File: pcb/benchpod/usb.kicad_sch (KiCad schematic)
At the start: 24 parts, among them U57 TPS259470ARPWR

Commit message: switched D1, added rules area with keepout
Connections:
- net +5V_EFUSE: now also D1.1 (K); no longer D1.2 (A)
- net GND: now also D1.2 (A); no longer D1.1 (K)
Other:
- moved on the sheet: D1
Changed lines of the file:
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@@
 	(symbol
 		(lib_id "lcsc_lib:SMAJ5.0A_C2925443")
-		(at 48.26 86.36 180)
+		(at 48.26 86.36 0)
 		(unit 1)
 		(body_style 1)
@@
 		)
 		(property "Footprint" "lcsc:SMA_L4.3-W2.6-LS5.0-RD"
-			(at 48.26 78.74 0)
+			(at 48.26 93.98 0)
 			(hide yes)
 			(show_name no)
@@
 		)
 		(property "Datasheet" "https://www.lcsc.com/datasheet/C2925443.pdf"
-			(at 48.26 76.2 0)
+			(at 48.26 96.52 0)
 			(hide yes)
 			(show_name no)
@@
 		)
 		(property "Manufacturer" "Liown(里阳半导体)"
-			(at 48.26 73.66 0)
+			(at 48.26 99.06 0)
 			(hide yes)
 			(show_name no)
@@
 		)
 		(property "MPN" "SMAJ5.0A"
-			(at 48.26 71.12 0)
+			(at 48.26 101.6 0)
 			(hide yes)
 			(show_name no)
@@
 		)
 		(property "LCSC Part" "C2925443"
-			(at 48.26 68.58 0)
+			(at 48.26 104.14 0)
 			(hide yes)
 			(show_name no)

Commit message: route cleanups and out of stock component replacement
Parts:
- C91, C92: footprint Capacitor_SMD:C_0603_1608Metric -> Capacitor_SMD:C_0805_2012Metric; LCSC C59461 -> C45783
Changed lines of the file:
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@@
 			)
 		)
-		(property "Footprint" "Capacitor_SMD:C_0603_1608Metric"
+		(property "Footprint" "Capacitor_SMD:C_0805_2012Metric"
 			(at 174.9552 148.59 0)
 			(hide yes)
@@
 			)
 		)
-		(property "LCSC" "C59461"
+		(property "LCSC" "C45783"
 			(at 173.99 144.78 0)
 			(hide yes)
@@
 			)
 		)
-		(property "Footprint" "Capacitor_SMD:C_0603_1608Metric"
+		(property "Footprint" "Capacitor_SMD:C_0805_2012Metric"
 			(at 186.3852 148.59 0)
 			(hide yes)
@@
 			)
 		)
-		(property "LCSC" "C59461"
+		(property "LCSC" "C45783"
 			(at 185.42 144.78 0)
 			(hide yes)

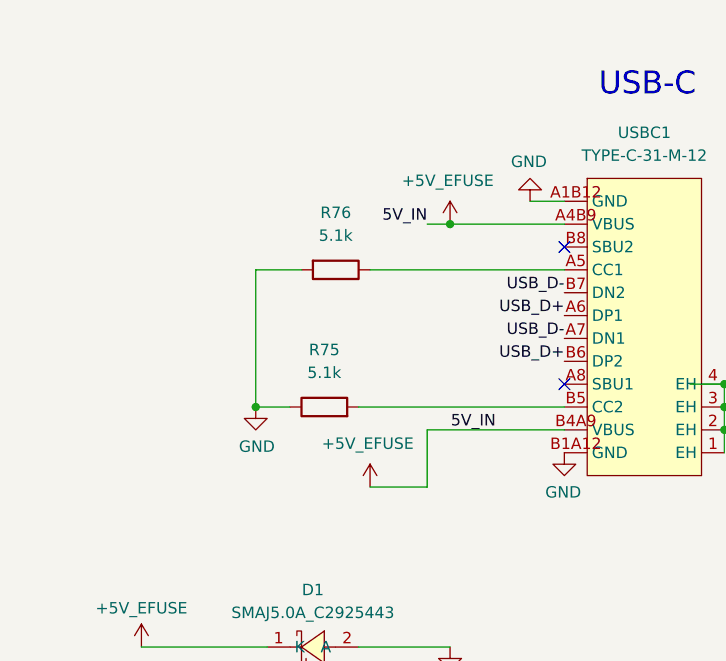
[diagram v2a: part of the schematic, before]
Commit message: fb changes, cc sensing, cleanups
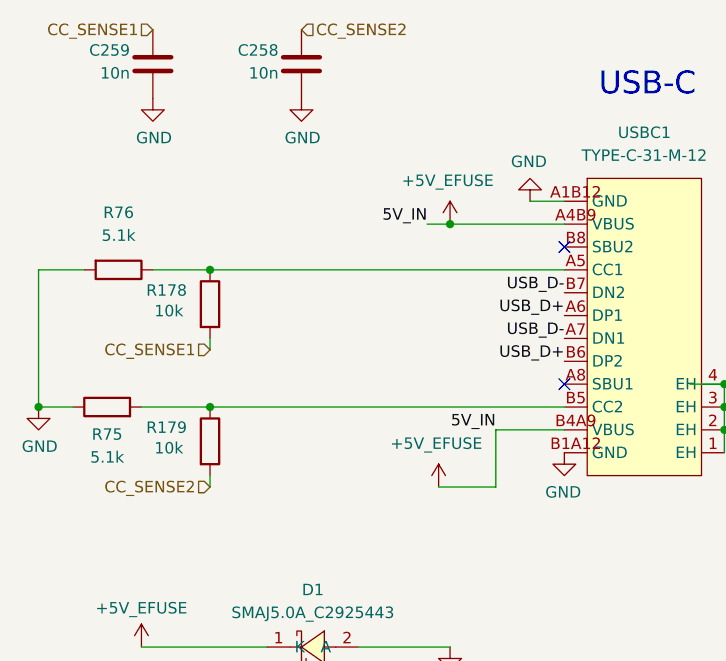
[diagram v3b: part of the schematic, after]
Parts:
- added C258, C259: 10n, Capacitor_SMD:C_0402_1005Metric, symbol Device:C
- added R178, R179: 10k, Resistor_SMD:R_0402_1005Metric, symbol Device:R
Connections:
- net GND: now also C258.2, C259.2
- net at R75.2, USBC1.B5 (CC2): now also R179.1
- net at R76.1, USBC1.A5 (CC1): now also R178.1
- new net CC_SENSE1: C259.1, R178.2
- new net CC_SENSE2: C258.1, R179.2
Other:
- moved on the sheet: R75, R76
